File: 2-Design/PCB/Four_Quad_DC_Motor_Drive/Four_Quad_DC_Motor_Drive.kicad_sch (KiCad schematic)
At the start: 0 parts

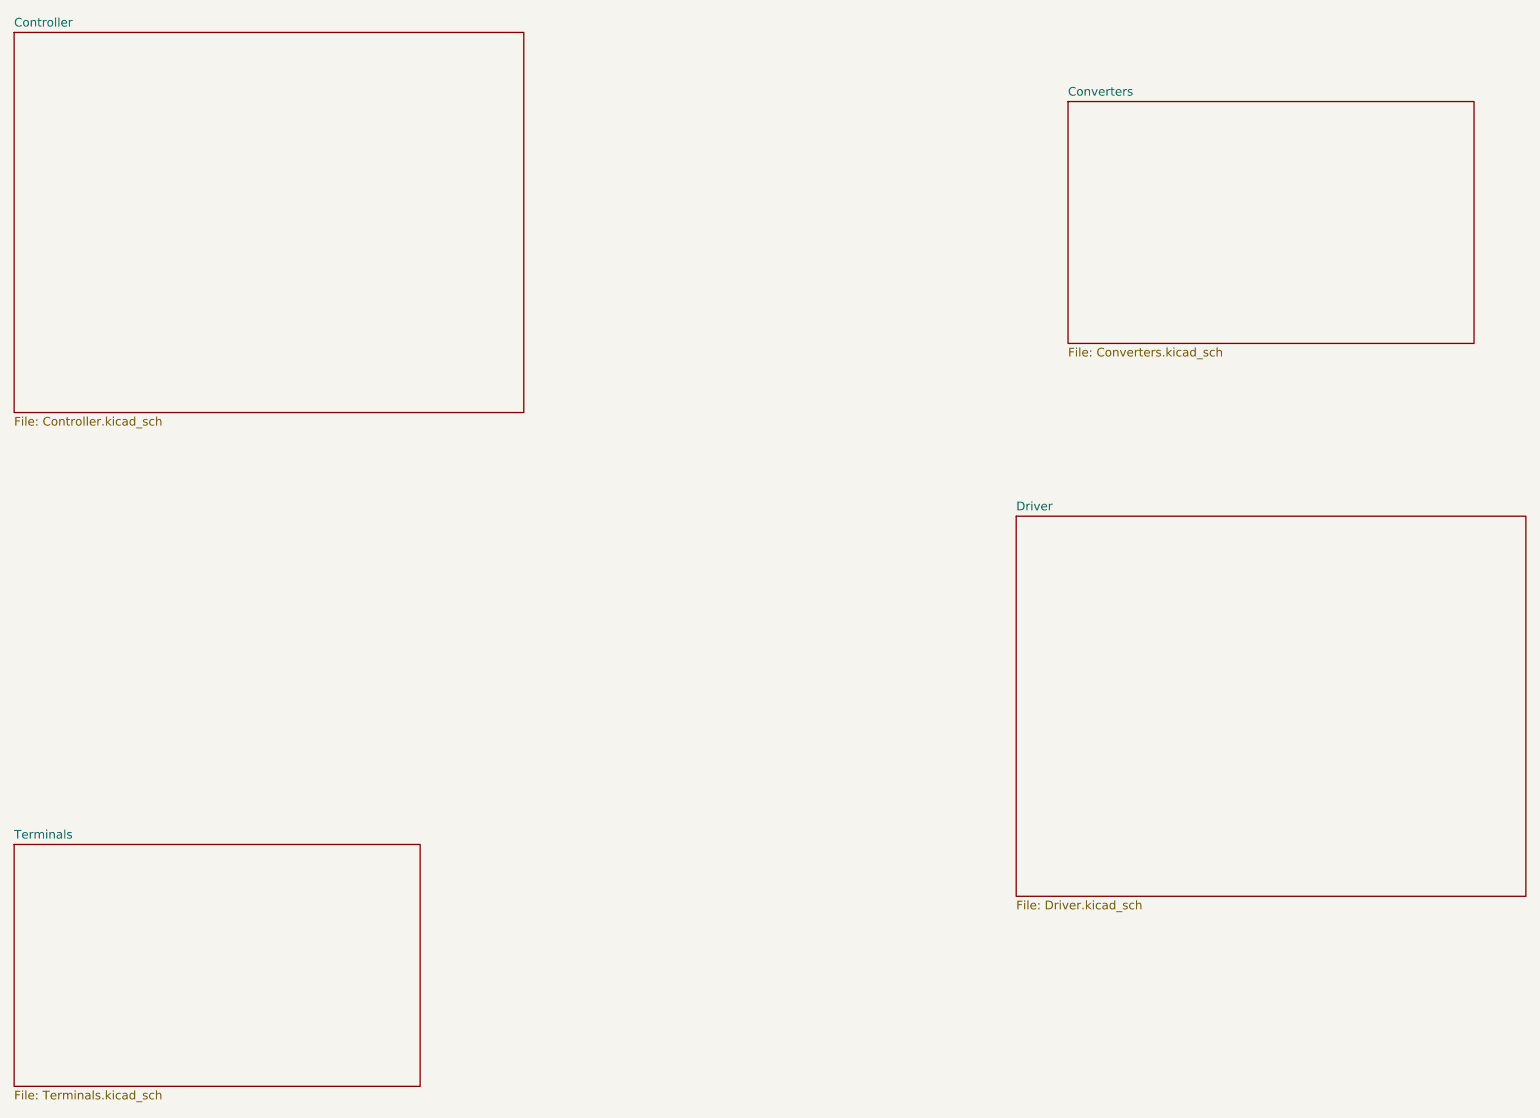
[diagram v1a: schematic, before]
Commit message: Added some more schematic symbols and three phase rectifier schematics
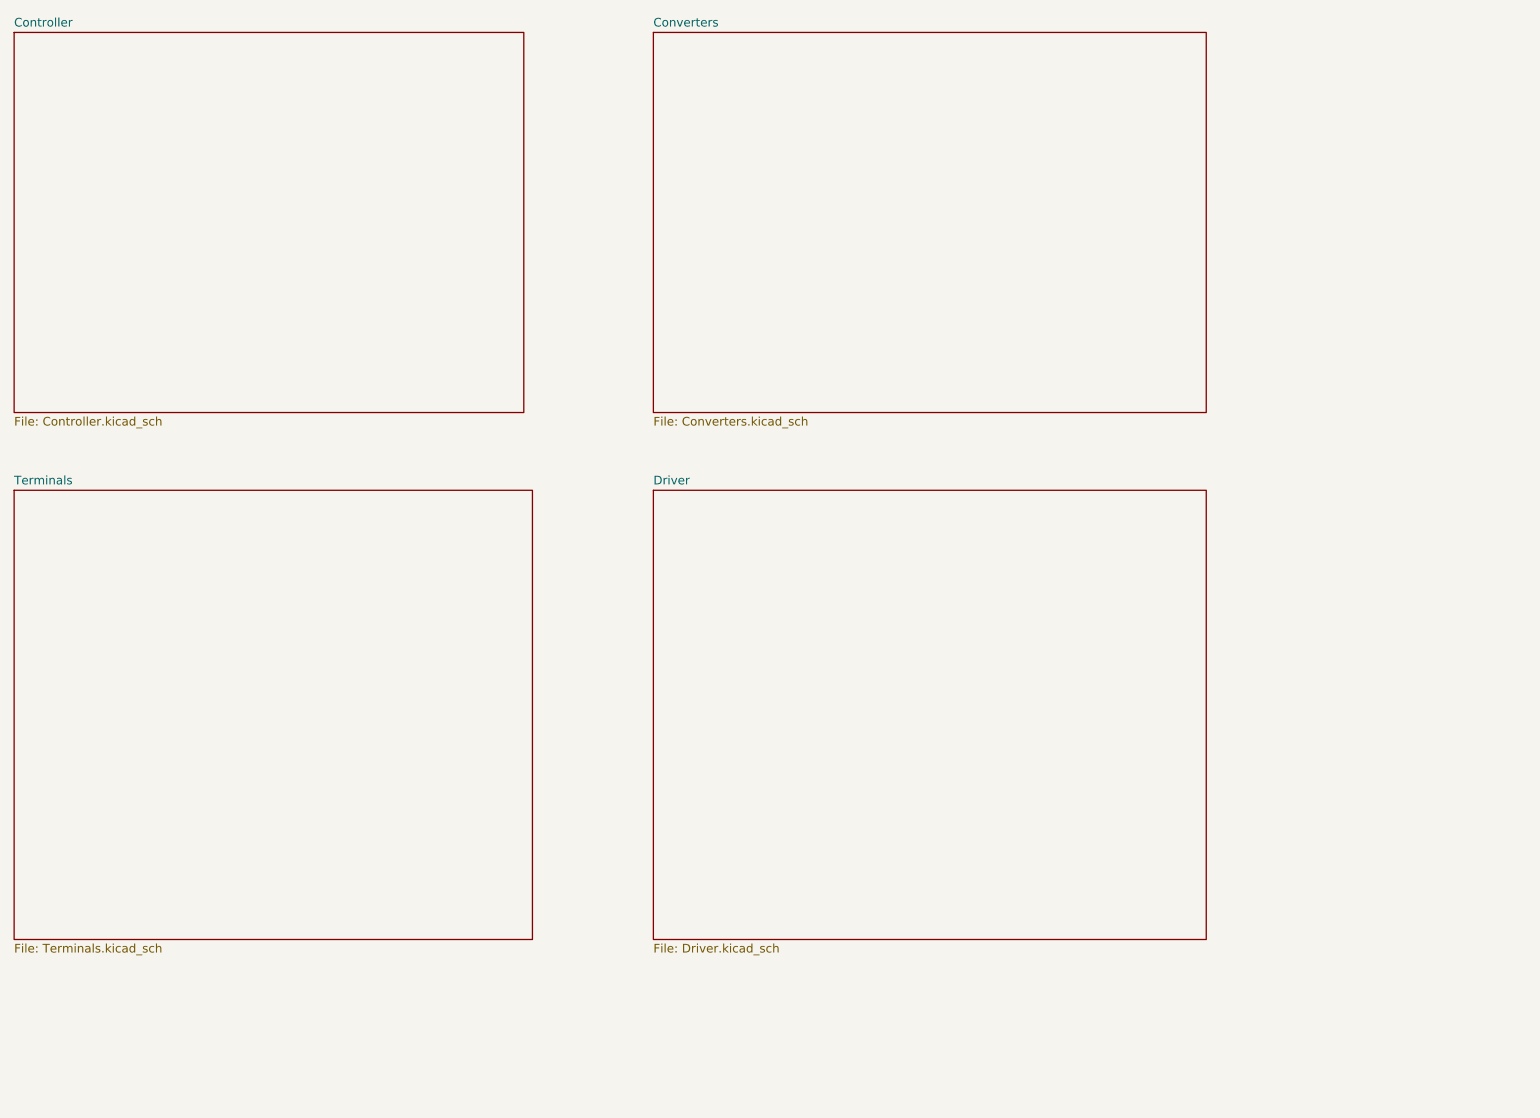
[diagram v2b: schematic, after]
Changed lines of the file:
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@@
 (kicad_sch (version 20211123) (generator eeschema)
   (paper "A4")
-  (sheet (at 34.29 140.97) (size 59.69 35.56) (fields_autoplaced)
+  (sheet (at 34.29 88.9) (size 76.2 66.04) (fields_autoplaced)
     (stroke (width 0.1524) (type solid) (color 0 0 0 0))
     (fill (color 0 0 0 0.0000))
-    (property "Sheet name" "Terminals" (id 0) (at 34.29 140.2584 0)
+    (property "Sheet name" "Terminals" (id 0) (at 34.29 88.1884 0)
       (effects (font (size 1.27 1.27)) (justify left bottom))
     )
-    (property "Sheet file" "Terminals.kicad_sch" (id 1) (at 34.29 177.1146 0)
+    (property "Sheet file" "Terminals.kicad_sch" (id 1) (at 34.29 155.5246 0)
       (effects (font (size 1.27 1.27)) (justify left top))
     )
   )
-  (sheet (at 181.61 92.71) (size 74.93 55.88) (fields_autoplaced)
+  (sheet (at 128.27 88.9) (size 81.28 66.04) (fields_autoplaced)
     (stroke (width 0.1524) (type solid) (color 0 0 0 0))
     (fill (color 0 0 0 0.0000))
-    (property "Sheet name" "Driver" (id 0) (at 181.61 91.9984 0)
+    (property "Sheet name" "Driver" (id 0) (at 128.27 88.1884 0)
       (effects (font (size 1.27 1.27)) (justify left bottom))
     )
-    (property "Sheet file" "Driver.kicad_sch" (id 1) (at 181.61 149.1746 0)
+    (property "Sheet file" "Driver.kicad_sch" (id 1) (at 128.27 155.5246 0)
       (effects (font (size 1.27 1.27)) (justify left top))
     )
@@
     )
   )
-  (sheet (at 189.23 31.75) (size 59.69 35.56) (fields_autoplaced)
+  (sheet (at 128.27 21.59) (size 81.28 55.88) (fields_autoplaced)
     (stroke (width 0.1524) (type solid) (color 0 0 0 0))
     (fill (color 0 0 0 0.0000))
-    (property "Sheet name" "Converters" (id 0) (at 189.23 31.0384 0)
+    (property "Sheet name" "Converters" (id 0) (at 128.27 20.8784 0)
       (effects (font (size 1.27 1.27)) (justify left bottom))
     )
-    (property "Sheet file" "Converters.kicad_sch" (id 1) (at 189.23 67.8946 0)
+    (property "Sheet file" "Converters.kicad_sch" (id 1) (at 128.27 78.0546 0)
       (effects (font (size 1.27 1.27)) (justify left top))
     )
@@
   )
   (symbol_instances
+    (path "/e96e6ae8-7a9c-4a62-9b76-177f281207af/abcf0e50-70ce-461b-8160-4dc7592eb878"
+      (reference "C?") (unit 1) (value "470uF") (footprint "")
+    )
+    (path "/562a4c0f-3180-4545-bb1e-8789c18066eb/07e01225-caa5-472c-bcc7-bddaed3e2cfe"
+      (reference "J?") (unit 1) (value "4mm_banana") (footprint "")
+    )
+    (path "/562a4c0f-3180-4545-bb1e-8789c18066eb/4041fdd9-73b0-4372-bcac-3e5150ff4421"
+      (reference "J?") (unit 1) (value "4mm_banana") (footprint "")
+    )
+    (path "/562a4c0f-3180-4545-bb1e-8789c18066eb/5e44c84e-9aff-4be1-a392-cecfed8b2fdf"
+      (reference "J?") (unit 1) (value "4mm_banana") (footprint "")
+    )
+    (path "/562a4c0f-3180-4545-bb1e-8789c18066eb/7f43cec7-e0cc-45a4-a352-542a84245111"
+      (reference "J?") (unit 1) (value "4mm_banana") (footprint "")
+    )
+    (path "/562a4c0f-3180-4545-bb1e-8789c18066eb/91febcc0-9806-45f8-a792-06eebb395735"
+      (reference "J?") (unit 1) (value "4mm_banana") (footprint "")
+    )
+    (path "/562a4c0f-3180-4545-bb1e-8789c18066eb/a0c9fce5-46ec-475e-9800-1b9103ff7fe0"
+      (reference "J?") (unit 1) (value "4mm_banana") (footprint "")
+    )
+    (path "/562a4c0f-3180-4545-bb1e-8789c18066eb/fd036163-cad0-4344-8f5c-5975c7793465"
+      (reference "J?") (unit 1) (value "4mm_banana") (footprint "")
+    )
     (path "/e96e6ae8-7a9c-4a62-9b76-177f281207af/c85b5131-d45f-4d34-b3c0-f1110780402b"
       (reference "U?") (unit 1) (value "SQL50") (footprint "")
